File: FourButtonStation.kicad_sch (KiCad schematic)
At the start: 66 parts, among them J1 AC IN, J10 AC IN, J11 AC IN, J2 External 3V, J3 UART, J4 ADC, J5 Conn_WallSocket, J6 USB_B_Micro, J7 Conn_WallSocket, J8 Conn_WallSocket, J9 Conn_WallSocket, K1 G5LE-1, K2 G5LE-1, K3 G5LE-1, K4 G5LE-1, Q1 MMBT3904, Q3 MMBT3904, SW1 POWER, SW2 RST, SW5 Mode, U1 CH340C, U10 SM4007PL, U11 D882_C9634, U13 AMS1117-3_3, U2 radio-receiver, U3 ESP-07, U4 SM4007PL, U5 D882_C9634, U6 SM4007PL, U7 D882_C9634, U8 SM4007PL, U9 D882_C9634

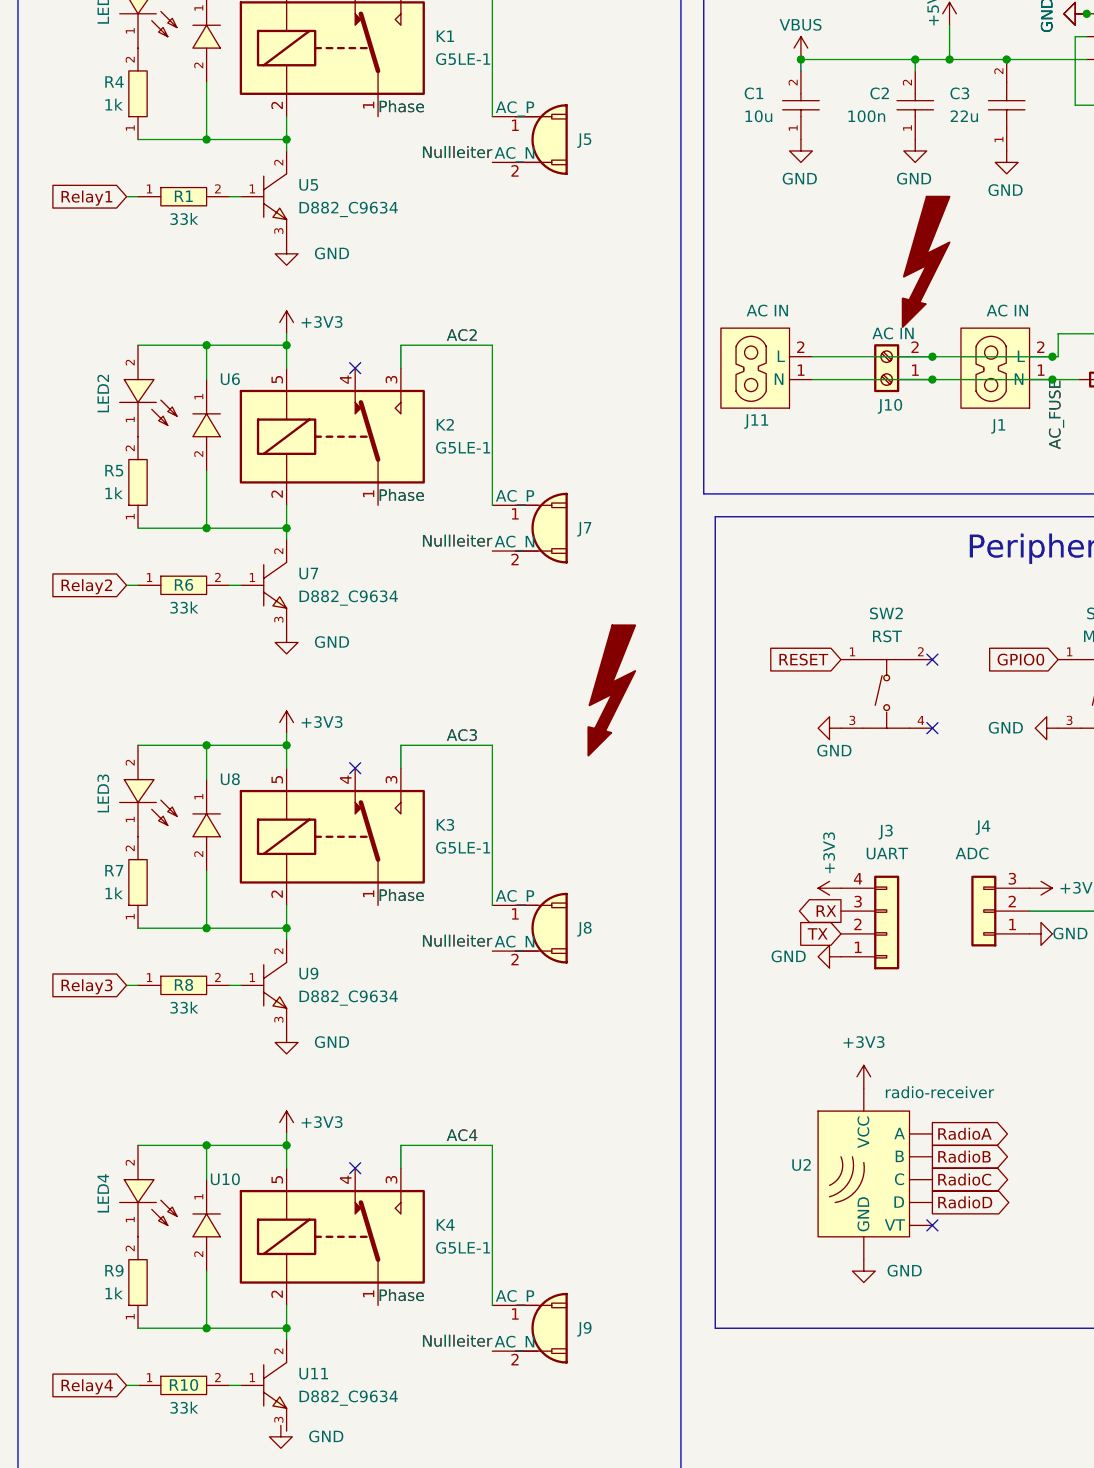
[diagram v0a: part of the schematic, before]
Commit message: Fix erroneously matched 1k resistors
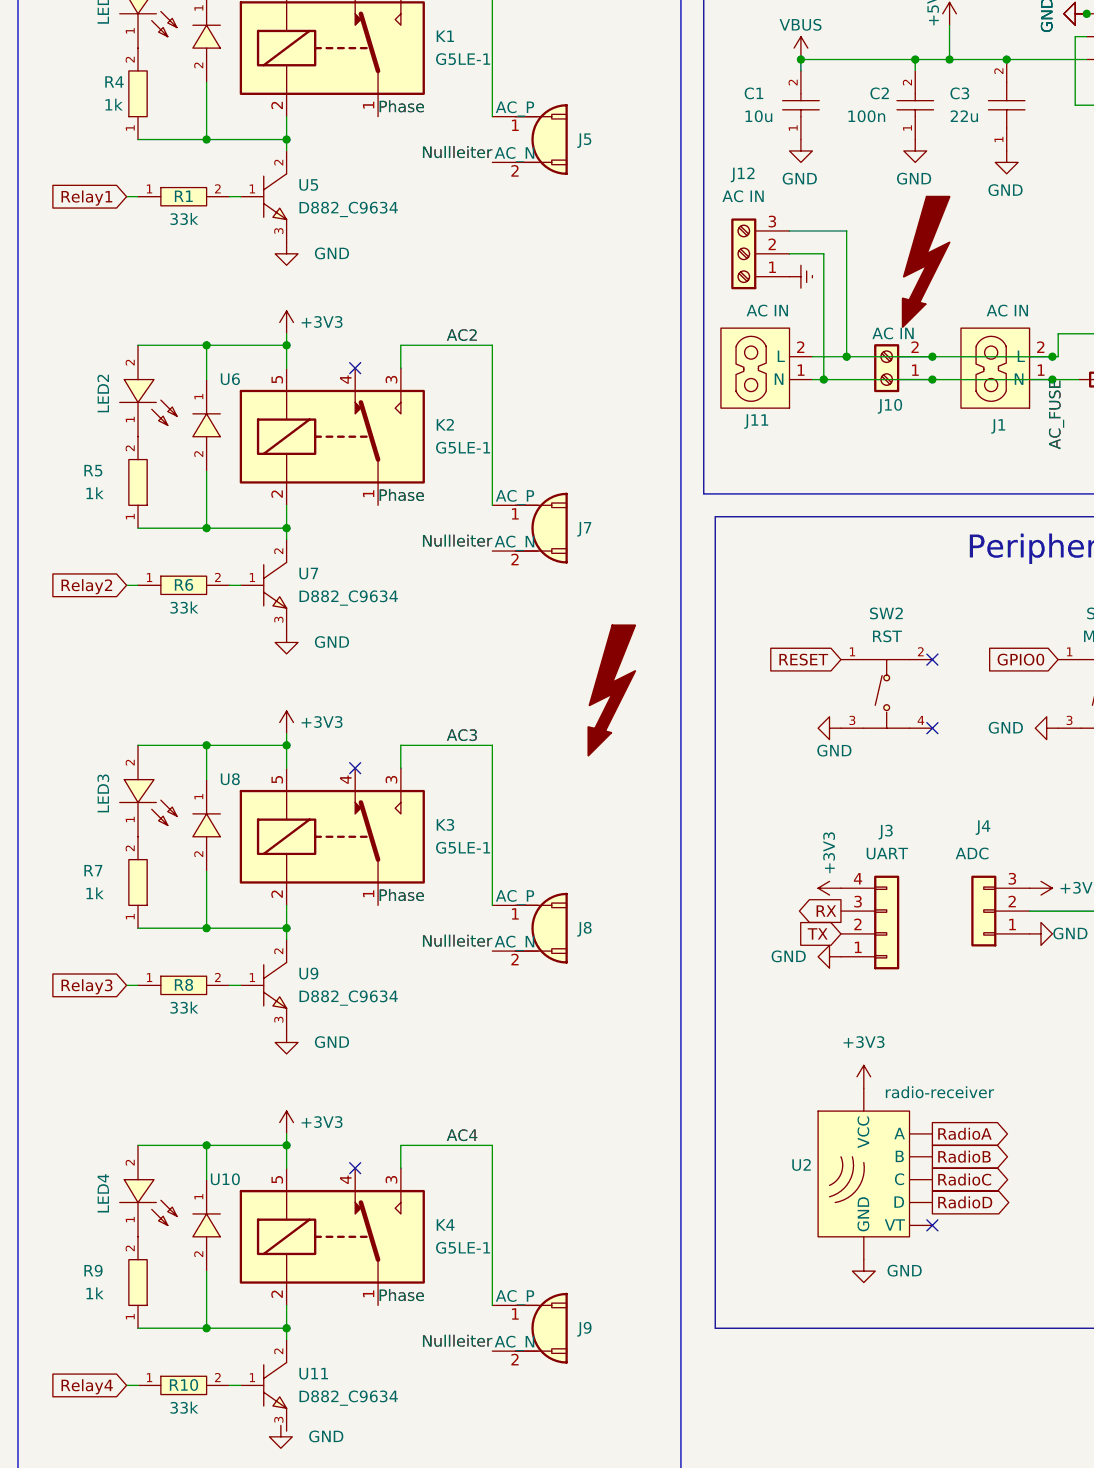
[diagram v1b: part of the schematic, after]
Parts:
- removed R4, R5, R7, R9: 1k, jlc_footprints:R0603, symbol jlc_symbols:0603WAF3302T5E
- added J12: AC IN, TerminalBlock_Phoenix:TerminalBlock_Phoenix_MKDS-1,5-3-5.08_1x03_P5.08mm_Horizontal, symbol Connector:Screw_Terminal_01x03
- added R4, R5, R7, R9: 1k, jlc_footprints:R0402, symbol jlc_symbols:0402WGF1001TCE
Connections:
- net AC_FUSE: now also J12.2 (Pin_2)
- net Phase: now also J12.3 (Pin_3)
- net at K4.2, U10.2 (A), U11.2 (C): now also R9.1
- net at LED4.1 (K): now also R9.2
- net at LED2.1 (K): now also R5.2
- net at LED3.1 (K): now also R7.2
- net at K1.2, U4.2 (A), U5.2 (C): now also R4.1
- net at K2.2, U6.2 (A), U7.2 (C): now also R5.1
- net at K3.2, U8.2 (A), U9.2 (C): now also R7.1
- net at LED1.1 (K): now also R4.2
- new net Earth: J12.1 (Pin_1)

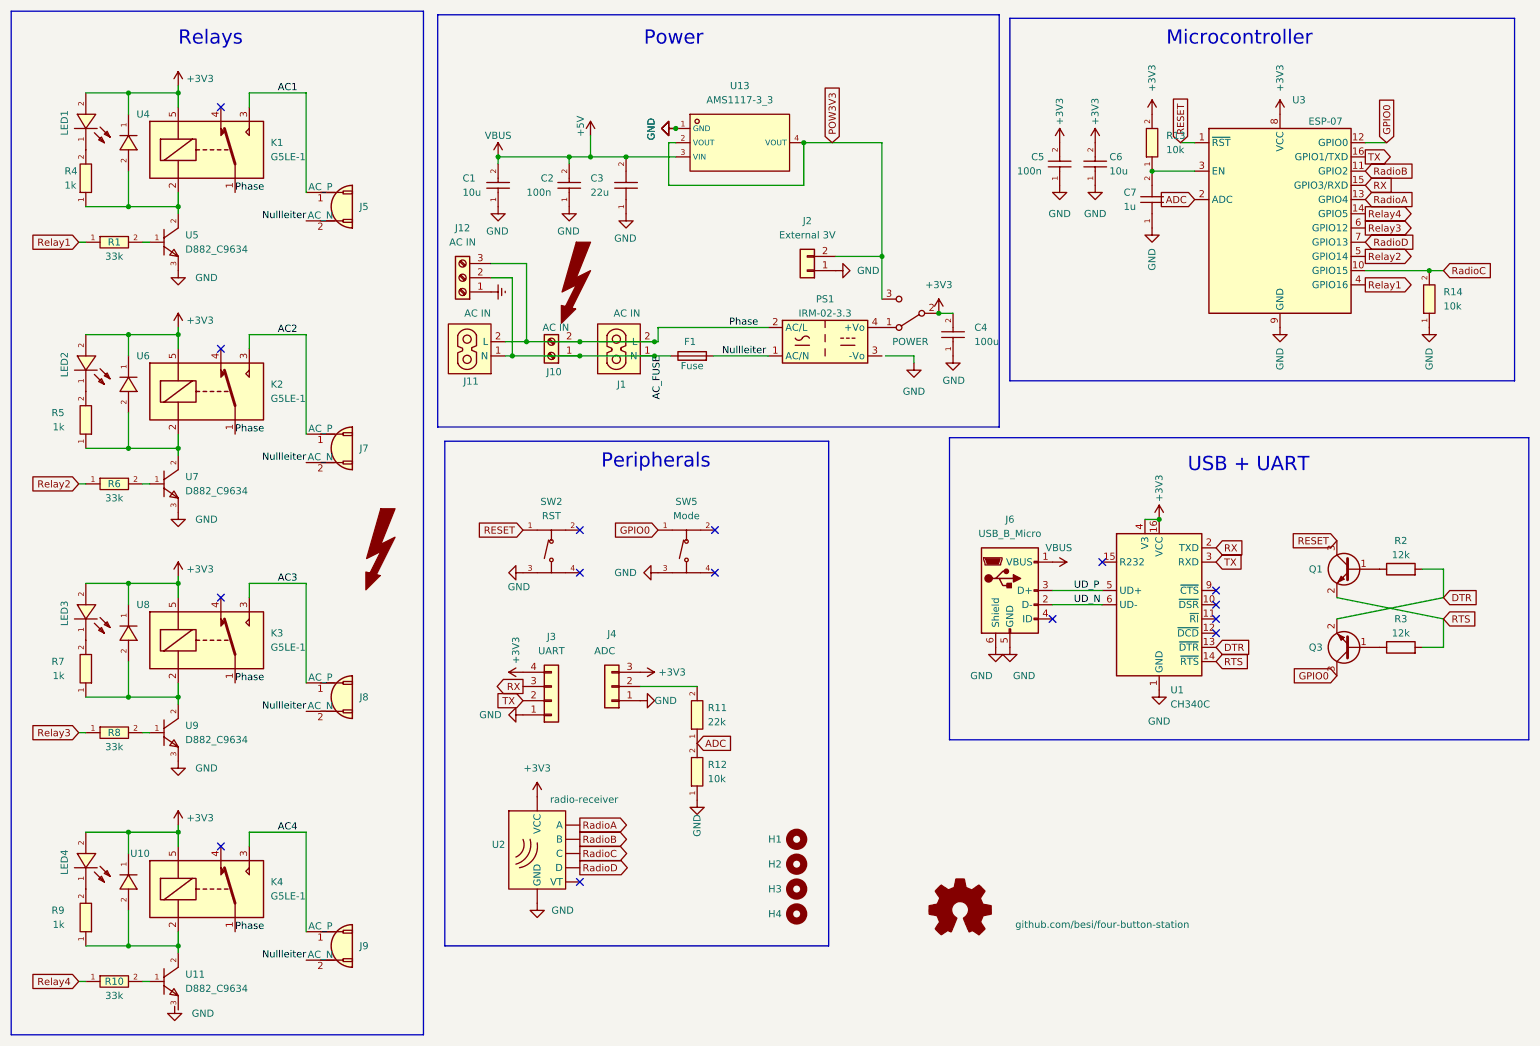
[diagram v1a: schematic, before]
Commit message: Rule checks and Silkscreen
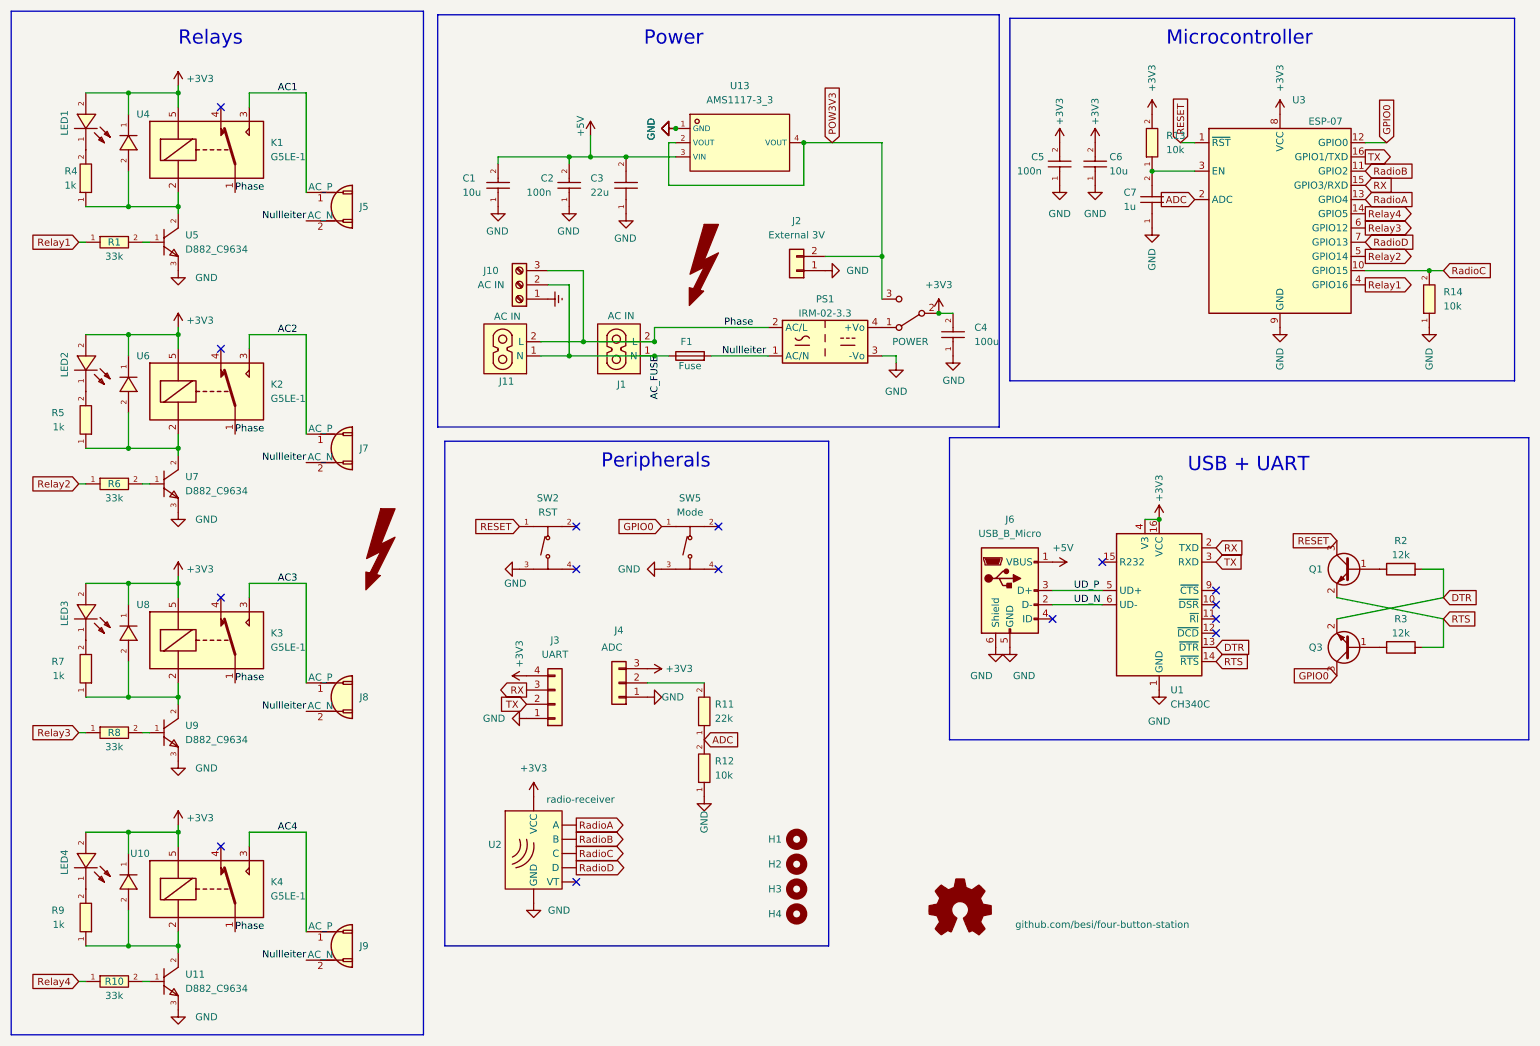
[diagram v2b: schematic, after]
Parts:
- removed J10: AC IN, TerminalBlock_Phoenix:TerminalBlock_Phoenix_MKDS-1,5-2_1x02_P5.00mm_Horizontal, symbol Connector:Screw_Terminal_01x02
- renumbered J12 to J10
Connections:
- net GND: now also PS1.3 (-Vo), U11.3 (E)
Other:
- moved on the sheet: J10, J11, J2, J3, J4, R11, R12, SW2, SW5, U2
